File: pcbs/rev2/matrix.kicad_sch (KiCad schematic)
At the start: 114 parts

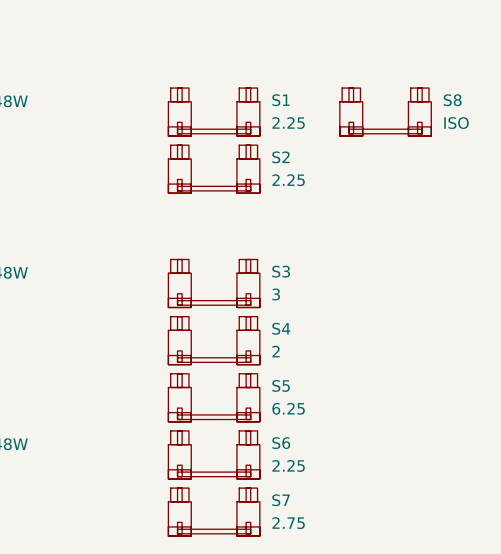
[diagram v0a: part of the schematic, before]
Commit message: Added 2u stab mount points for 3u Spacebar option
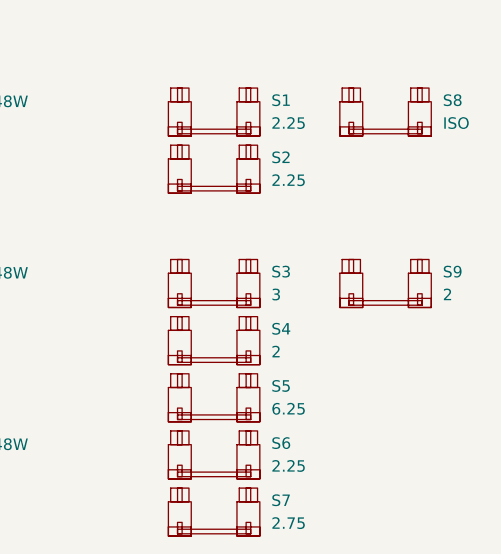
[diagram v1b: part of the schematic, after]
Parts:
- added S9: 2, PCM_marbastlib-mx:STAB_MX_2u, symbol PCM_marbastlib-mx:MX_stab
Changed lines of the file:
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@@
+	)
+	(symbol
+		(lib_id "PCM_marbastlib-mx:MX_stab")
+		(at 218.44 77.47 0)
+		(unit 1)
+		(exclude_from_sim no)
+		(in_bom yes)
+		(on_board yes)
+		(dnp no)
+		(fields_autoplaced yes)
+		(property "Reference" "S9"
+			(at 224.79 76.0729 0)
+			(effects
+				(font
+					(size 1.27 1.27)
+				)
+				(justify left)
+			)
+		)
+		(property "Value" "2"
+			(at 224.79 78.6129 0)
+			(effects
+				(font
+					(size 1.27 1.27)
+				)
+				(justify left)
+			)
+		)
+		(property "Footprint" "PCM_marbastlib-mx:STAB_MX_2u"
+			(at 218.44 77.47 0)
+			(effects
+				(font
+					(size 1.27 1.27)
+				)
+				(hide yes)
+			)
+		)
+		(property "Datasheet" ""
+			(at 218.44 77.47 0)
+			(effects
+				(font
+					(size 1.27 1.27)
+				)
+				(hide yes)
+			)
+		)
+		(property "Description" ""
+			(at 218.44 77.47 0)
+			(effects
+				(font
+					(size 1.27 1.27)
+				)
+				(hide yes)
+			)
+		)
+		(instances
+			(project "bonk"
+				(path "/3657237e-c8f2-4ecf-b631-303d8d00a2b6/86c11717-6fb1-49fa-ba22-57d9c11d0559"
+					(reference "S9")
+					(unit 1)
+				)
+			)
+		)
 	)
 	(symbol
